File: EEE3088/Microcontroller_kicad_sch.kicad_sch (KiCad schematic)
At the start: 1 part, among them U1 STM32F051C6Tx

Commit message: First night - c
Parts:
- added C3, C5: 100nF, symbol Device:C
- added C4: 10nF, symbol Device:C
- added C6: 4.7uF, symbol Device:C
- added C7: 1uF, symbol Device:C
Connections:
- net GND: now reaches U1.23 (VSS), U1.47 (VSS)
- net GND: now also U1.8 (VSSA), C3.2, C4.2, C5.2, C6.2, C7.2
- net +3.3V: now reaches U1.24 (VDD)
- net +3.3V: now also U1.48 (VDD), U1.9 (VDDA), C3.1, C4.1, C5.1, C6.1, C7.1

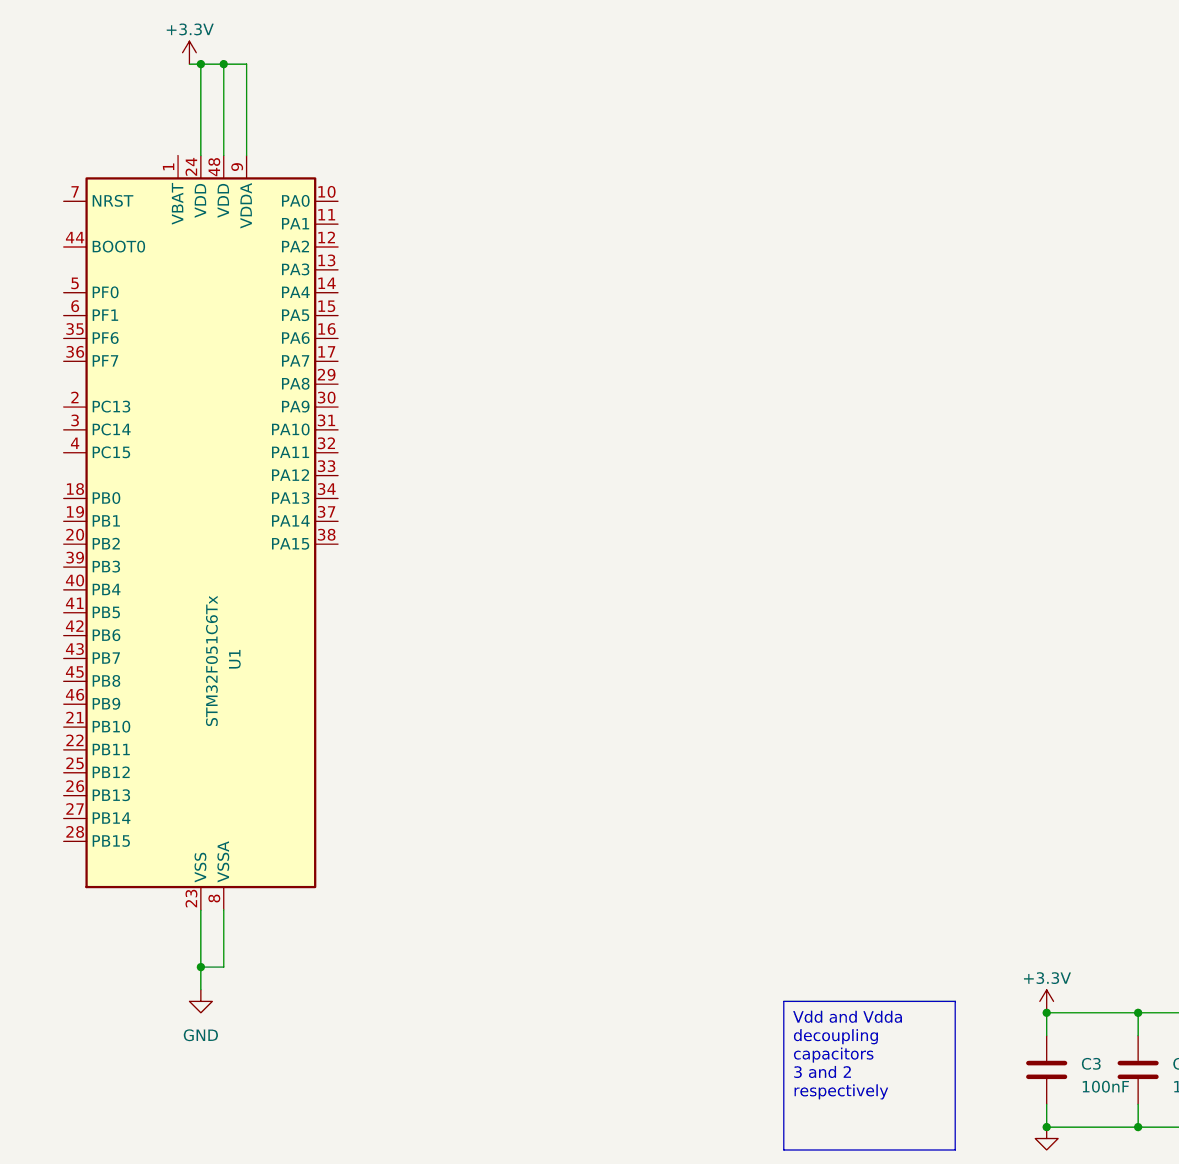
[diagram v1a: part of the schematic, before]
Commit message: Microcontroller Comms
Finished my subsection
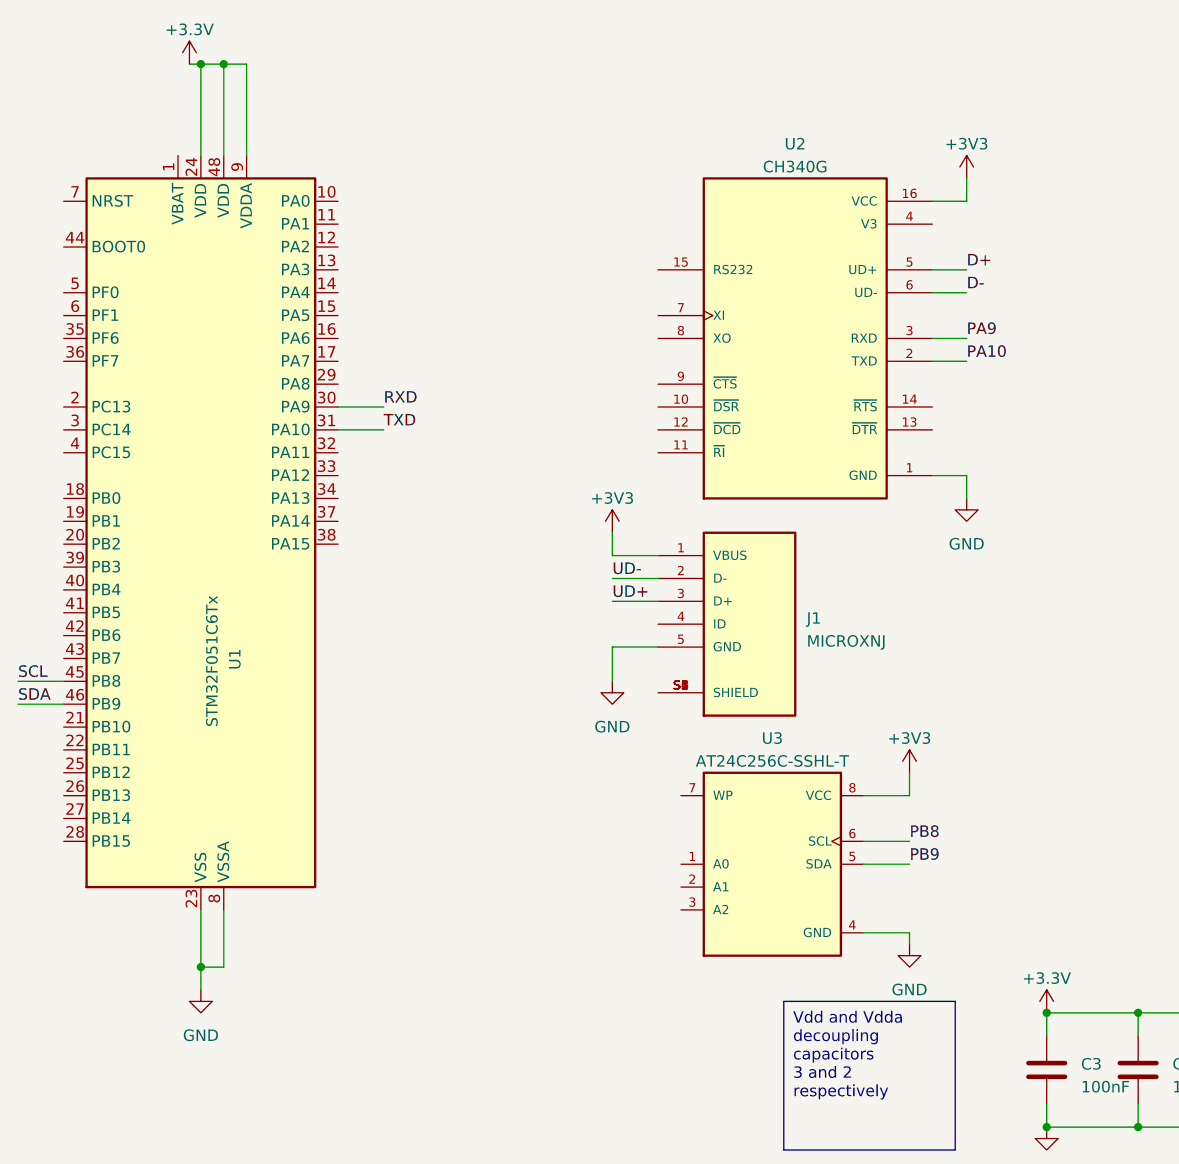
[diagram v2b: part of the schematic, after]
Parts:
- added J1: MICROXNJ, SHOUHAN_MICROXNJ, symbol MICROXNJ:MICROXNJ
- added U2: CH340G, SOIC127P600X180-16N, symbol CH340G:CH340G
- added U3: AT24C256C-SSHL-T, SOIC127P600X175-8N, symbol AT24C256C-SSHL-T:AT24C256C-SSHL-T
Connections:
- net GND: now also J1.5 (GND), U2.1 (GND), U3.4 (GND)
- net RXD: now reaches U1.30 (PA9)
- net TXD: now reaches U1.31 (PA10)
- net SCL: now reaches U1.45 (PB8)
- net SDA: now reaches U1.46 (PB9)
- new net: J1.S1 (SHIELD), J1.S2 (SHIELD), J1.S3 (SHIELD), J1.S4 (SHIELD), J1.S5 (SHIELD), J1.S6 (SHIELD)
- new net +3V3: J1.1 (VBUS), U2.16 (VCC), U3.8 (VCC)
- new net D+: U2.5 (UD+)
- new net D-: U2.6 (UD-)
- new net PA10: U2.2 (TXD)
- new net PA9: U2.3 (RXD)
- new net PB8: U3.6 (SCL)
- new net PB9: U3.5 (SDA)
- new net UD+: J1.3 (D+)
- new net UD-: J1.2 (D-)

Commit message: 05/03
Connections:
- net RXD is gone; now on net USB_RXD: U1.30 (PA9)
- net SCL is gone; now on net EEPROM_SCL: U1.45 (PB8)
- net SDA is gone; now on net EEPROM_SDA: U1.46 (PB9)
- net TXD is gone; now on net USB_TXD: U1.31 (PA10)
- net UD+ is gone; now on net USB_D+: J1.3 (D+)
- net UD- is gone; now on net USB_D-: J1.2 (D-)
- net GND: now also J1.S1 (SHIELD), J1.S2 (SHIELD), J1.S3 (SHIELD), J1.S4 (SHIELD), J1.S5 (SHIELD), J1.S6 (SHIELD), U3.7 (WP)
- net EEPROM_A0: now reaches U3.1 (A0)
- net EEPROM_A1: now reaches U3.2 (A1)
- net EEPROM_A2: now reaches U3.3 (A2)
- net NC: now reaches J1.4 (ID)
- net D+ renamed USB_D+
- net D- renamed USB_D-
- net PA10 renamed USB_TXD
- net PA9 renamed USB_RXD
- net PB8 renamed EEPROM_SCL
- net PB9 renamed EEPROM_SDA
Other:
- moved on the sheet: J1, U2, U3

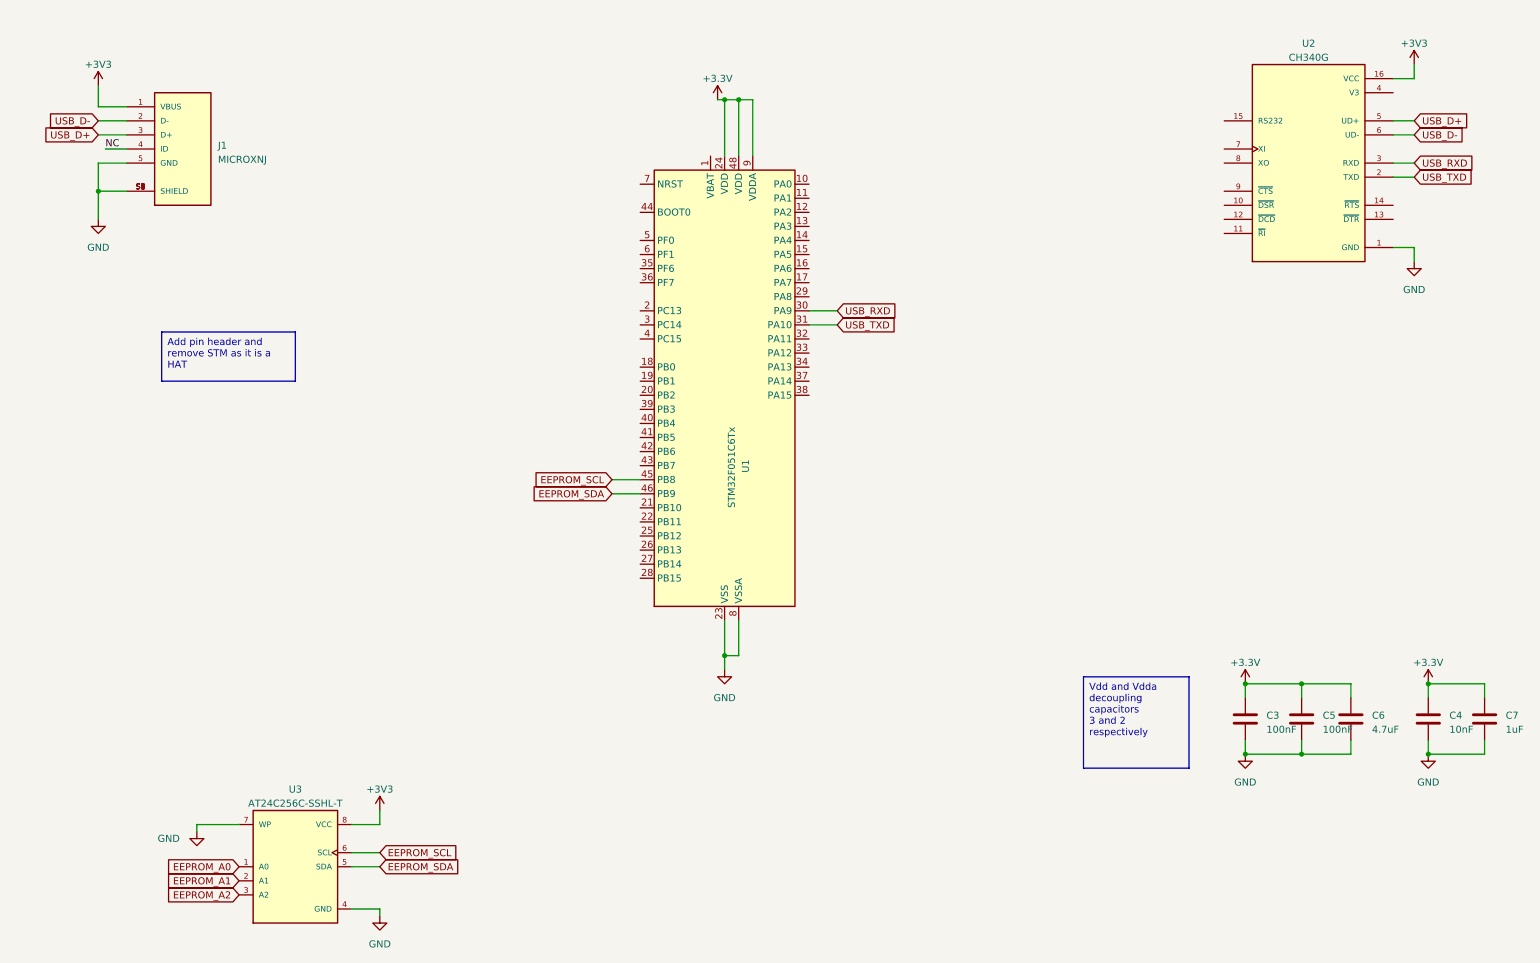
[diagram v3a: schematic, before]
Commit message: Proposal update
Power update
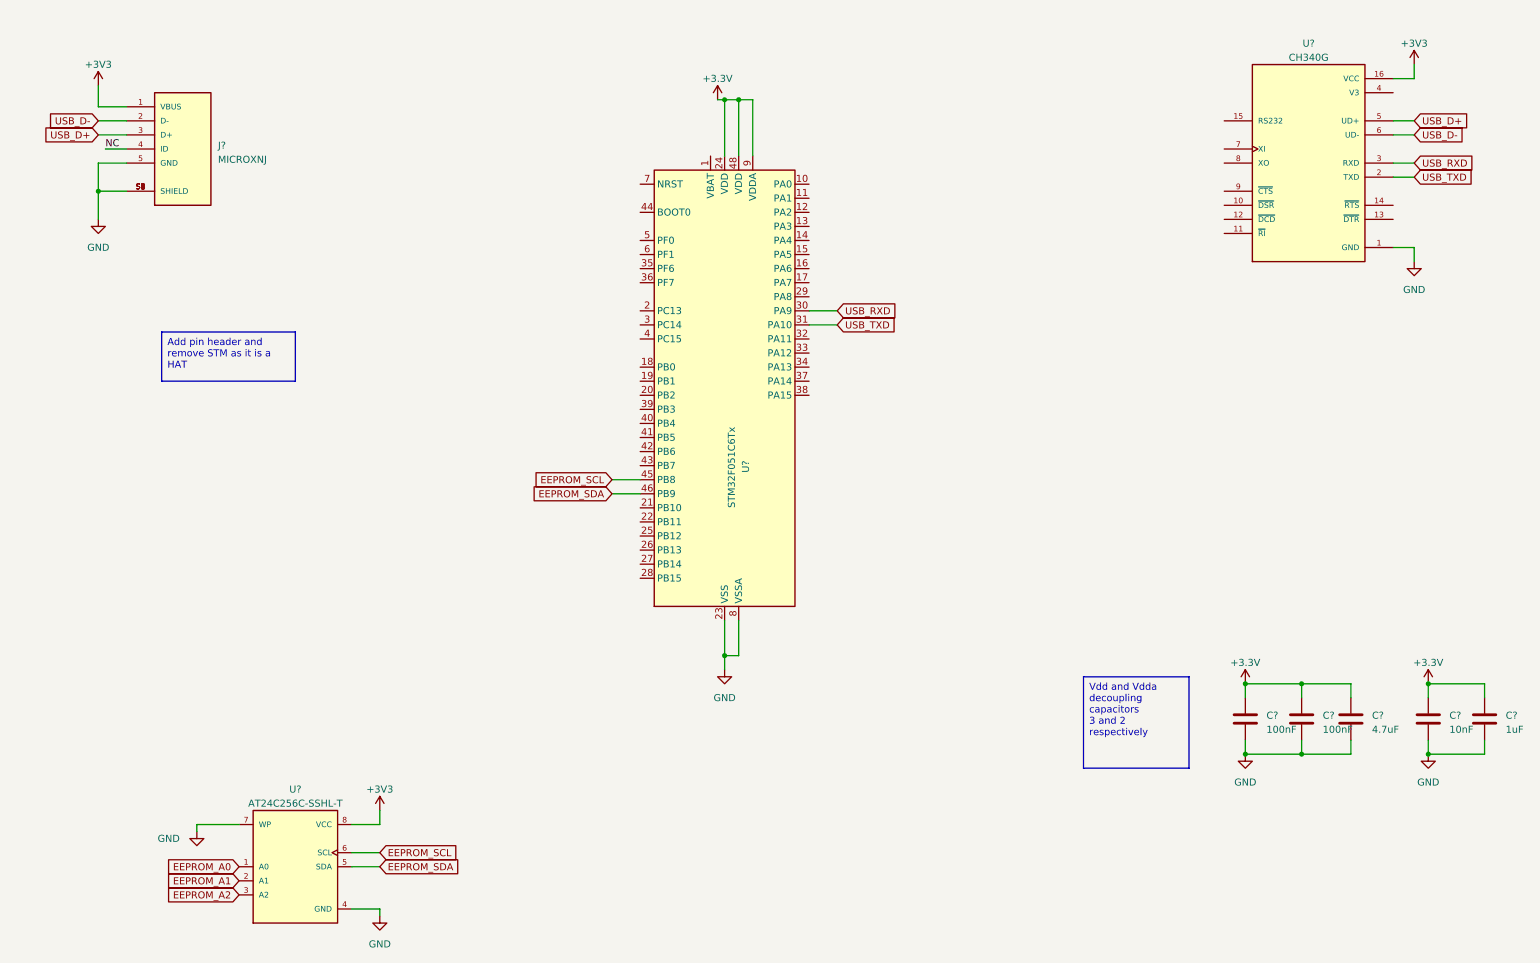
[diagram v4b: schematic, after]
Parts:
- renumbered C7 to C?, C3 to C?, C6 to C?, C4 to C?, C5 to C?, J1 to J?, U3 to U?, U2 to U?, U1 to U?

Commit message: Power update
included Low voltage reg
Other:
- company: (none) -> UCT
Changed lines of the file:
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@@
 (kicad_sch (version 20230121) (generator eeschema)
   (paper "A4")
+  (title_block
+    (company "UCT")
+  )
   (junction (at 140.97 33.02) (diameter 0) (color 0 0 0 0)
   )
@@
       (effects (font (size 1.27 1.27)) hide)
     )
+    (property "Price" "" (at 278.13 144.78 0)
+      (effects (font (size 1.27 1.27)) hide)
+    )
+    (property "Basic" "" (at 278.13 144.78 0)
+      (effects (font (size 1.27 1.27)) hide)
+    )
+    (property "Extended" "" (at 278.13 144.78 0)
+      (effects (font (size 1.27 1.27)) hide)
+    )
     (pin "1")
     (pin "2")
@@
     (property "MANUFACTURER" "Atmel" (at 63.5 171.45 0)
       (effects (font (size 1.27 1.27)) (justify bottom) hide)
+    )
+    (property "Price" "" (at 63.5 171.45 0)
+      (effects (font (size 1.27 1.27)) hide)
+    )
+    (property "Basic" "" (at 63.5 171.45 0)
+      (effects (font (size 1.27 1.27)) hide)
+    )
+    (property "Extended" "" (at 63.5 171.45 0)
+      (effects (font (size 1.27 1.27)) hide)
     )
     (pin "1")
@@
     (property "MAXIMUM_PACKAGE_HEIGHT" "1.8 mm" (at 246.38 44.45 0)
       (effects (font (size 1.27 1.27)) (justify bottom) hide)
+    )
+    (property "Price" "" (at 246.38 44.45 0)
+      (effects (font (size 1.27 1.27)) hide)
+    )
+    (property "Basic" "" (at 246.38 44.45 0)
+      (effects (font (size 1.27 1.27)) hide)
+    )
+    (property "Extended" "" (at 246.38 44.45 0)
+      (effects (font (size 1.27 1.27)) hide)
     )
     (pin "1")
@@
       (effects (font (size 1.27 1.27)) (justify bottom) hide)
     )
+    (property "Price" "" (at 43.18 41.91 0)
+      (effects (font (size 1.27 1.27)) hide)
+    )
+    (property "Basic" "" (at 43.18 41.91 0)
+      (effects (font (size 1.27 1.27)) hide)
+    )
+    (property "Extended" "" (at 43.18 41.91 0)
+      (effects (font (size 1.27 1.27)) hide)
+    )
     (pin "1")
     (pin "2")
@@
       (effects (font (size 1.27 1.27)) hide)
     )
+    (property "Price" "" (at 234.95 144.78 0)
+      (effects (font (size 1.27 1.27)) hide)
+    )
+    (property "Basic" "" (at 234.95 144.78 0)
+      (effects (font (size 1.27 1.27)) hide)
+    )
+    (property "Extended" "" (at 234.95 144.78 0)
+      (effects (font (size 1.27 1.27)) hide)
+    )
     (pin "1")
     (pin "2")
@@
     )
     (property "Datasheet" "https://www.st.com/resource/en/datasheet/stm32f051c6.pdf" (at 140.97 86.36 0)
+      (effects (font (size 1.27 1.27)) hide)
+    )
+    (property "Price" "" (at 140.97 86.36 0)
+      (effects (font (size 1.27 1.27)) hide)
+    )
+    (property "Basic" "" (at 140.97 86.36 0)
+      (effects (font (size 1.27 1.27)) hide)
+    )
+    (property "Extended" "" (at 140.97 86.36 0)
       (effects (font (size 1.27 1.27)) hide)
     )
@@
       (effects (font (size 1.27 1.27)) hide)
     )
+    (property "Price" "" (at 254 144.78 0)
+      (effects (font (size 1.27 1.27)) hide)
+    )
+    (property "Basic" "" (at 254 144.78 0)
+      (effects (font (size 1.27 1.27)) hide)
+    )
+    (property "Extended" "" (at 254 144.78 0)
+      (effects (font (size 1.27 1.27)) hide)
+    )
     (pin "1")
     (pin "2")
@@
       (effects (font (size 1.27 1.27)) hide)
     )
+    (property "Price" "" (at 267.97 144.78 0)
+      (effects (font (size 1.27 1.27)) hide)
+    )
+    (property "Basic" "" (at 267.97 144.78 0)
+      (effects (font (size 1.27 1.27)) hide)
+    )
+    (property "Extended" "" (at 267.97 144.78 0)
+      (effects (font (size 1.27 1.27)) hide)
+    )
     (pin "1")
     (pin "2")
@@
       (effects (font (size 1.27 1.27)) hide)
     )
+    (property "Price" "" (at 245.11 144.78 0)
+      (effects (font (size 1.27 1.27)) hide)
+    )
+    (property "Basic" "" (at 245.11 144.78 0)
+      (effects (font (size 1.27 1.27)) hide)
+    )
+    (property "Extended" "" (at 245.11 144.78 0)
+      (effects (font (size 1.27 1.27)) hide)
+    )

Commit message: Rev_1_compl.
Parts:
- C?: footprint (none) -> CL21B105KBFNNNE; Extended (none) -> 0; Price (none) -> 0.0087
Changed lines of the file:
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@@
       (effects (font (size 1.27 1.27)) (justify left))
     )
-    (property "Footprint" "" (at 279.0952 148.59 0)
+    (property "Footprint" "CL21B105KBFNNNE" (at 279.0952 148.59 0)
       (effects (font (size 1.27 1.27)) hide)
     )
-    (property "Datasheet" "~" (at 278.13 144.78 0)
+    (property "Datasheet" "https://datasheet.lcsc.com/lcsc/1810191216_Samsung-Electro-Mechanics-CL21B105KBFNNNE_C28323.pdf" (at 278.13 144.78 0)
       (effects (font (size 1.27 1.27)) hide)
     )
-    (property "Price" "" (at 278.13 144.78 0)
+    (property "Price" "0.0087" (at 278.13 144.78 0)
       (effects (font (size 1.27 1.27)) hide)
     )
@@
       (effects (font (size 1.27 1.27)) hide)
     )
-    (property "Extended" "" (at 278.13 144.78 0)
+    (property "Extended" "0" (at 278.13 144.78 0)
       (effects (font (size 1.27 1.27)) hide)
     )
+    (property "Description" "1uF Cap 0805" (at 278.13 144.78 0)
+      (effects (font (size 1.27 1.27)) hide)
+    )
